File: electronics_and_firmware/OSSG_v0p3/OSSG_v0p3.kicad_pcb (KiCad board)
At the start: 4 copper layers, 85 x 9 mm, 61 parts, among them IC1 DW01A, J1 USB_B_Micro, Q1 FS8205A, Q2 Q_NPN_BEC, Q3 Q_NPN_BEC, SW1 SW_SPST, U1 ESP32-PICO-D4, U2 TP4056, U3 XC6222B331MRG, U4 FT232RQ

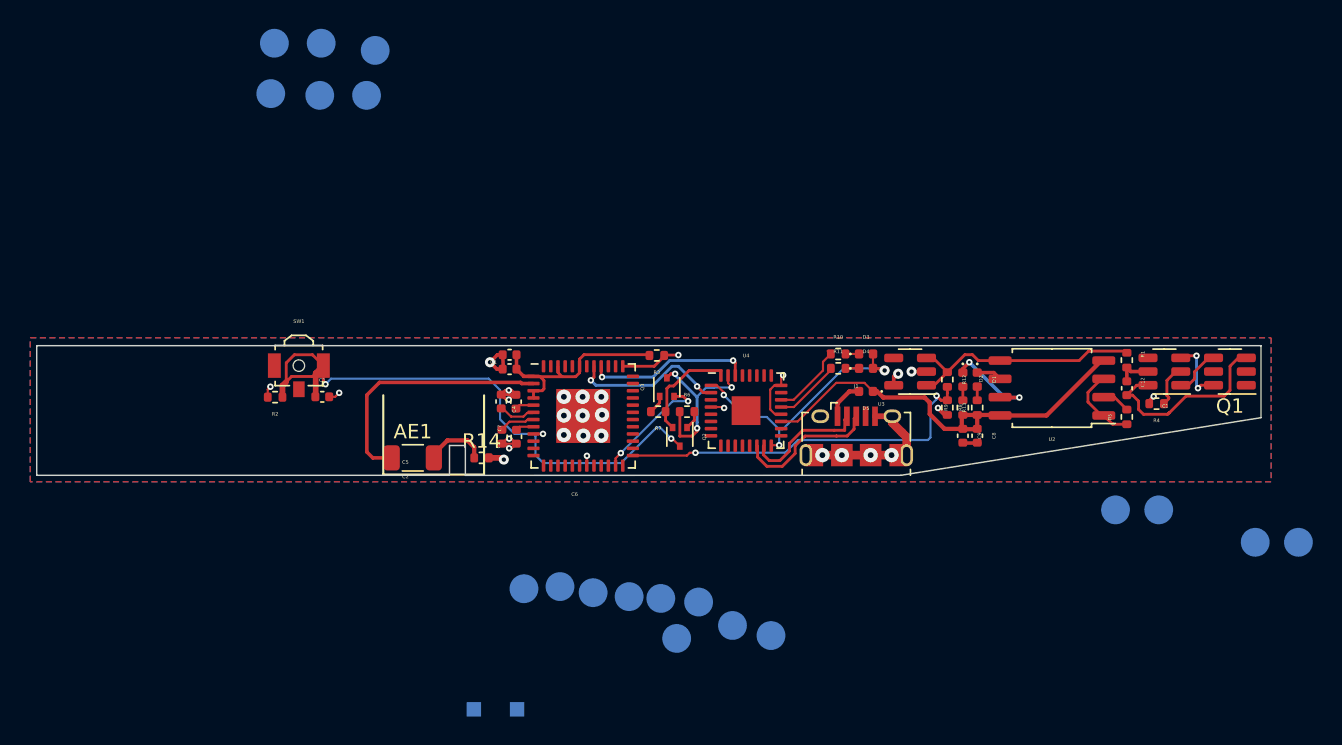
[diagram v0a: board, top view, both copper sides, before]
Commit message: change breakout test pads footprint size and start laying out breakouts
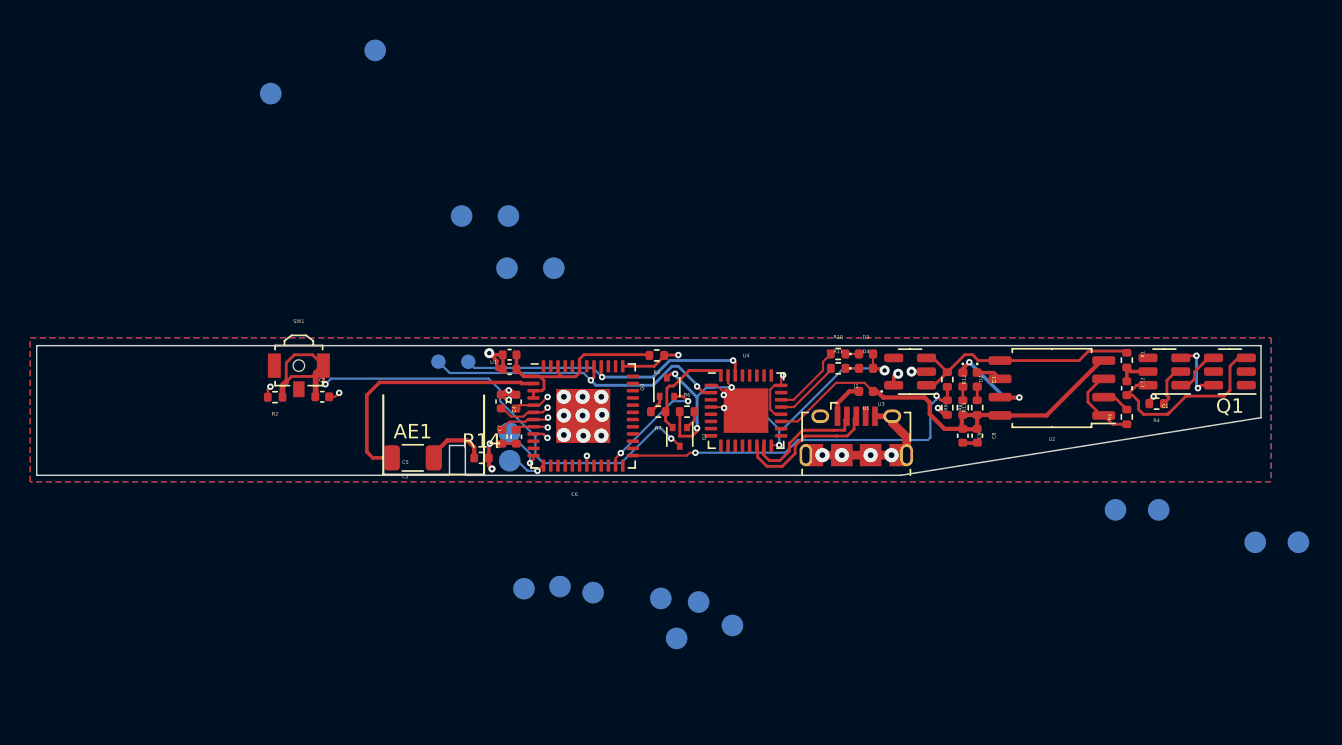
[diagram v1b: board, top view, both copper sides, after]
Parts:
- TP22: value IO15_SPI2_MISO -> IO23_BO
- TP24: value IO17_U2TXD -> IO33_BO
- TP3, TP4: footprint TestPoint:TestPoint_Pad_1.0x1.0mm -> TestPoint:TestPoint_Pad_D1.0mm
- moved TP4 24.4 mm to (105.0, 76.1)
- moved TP3 24.3 mm to (102.9, 76.1)
- moved TP24 21.8 mm to (107.8, 83.0)
- moved TP12 17.7 mm to (110.9, 69.6)
- moved TP2 17.7 mm to (107.7, 69.6)
- moved TP10 17.7 mm to (104.5, 66.0)
- moved TP11 17.7 mm to (107.8, 66.0)
- moved TP22 14.1 mm to (107.8, 81.1)
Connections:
- TP22 pad 1: IO12 -> IO32
- TP24 pad 1: IO17 -> IO33
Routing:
- net VCCIO: track 18.8 -> 31.9 mm, vias 3 -> 7
- net DTR: track 12.2 -> 0.00 mm, vias 3 -> 0
- net TX_ESP: track 10.9 -> 22.1 mm
- net RX_ESP: track 11.4 -> 21.1 mm
- net IO32: track 0.00 -> 3.32 mm, vias 0 -> 1
- net IO33: track 0.00 -> 2.31 mm, vias 0 -> 1
- net ADC1C2: track 1.31 -> 2.53 mm, vias 0 -> 1
- net ADC1C0: track 2.60 -> 3.71 mm, vias 0 -> 1
- net ADC1C1: track 2.51 -> 3.58 mm, vias 0 -> 1
- net ADC1C3: track 1.28 -> 2.29 mm, vias 0 -> 1
- net GND: track 36.9 -> 36.7 mm, vias 25 -> 23

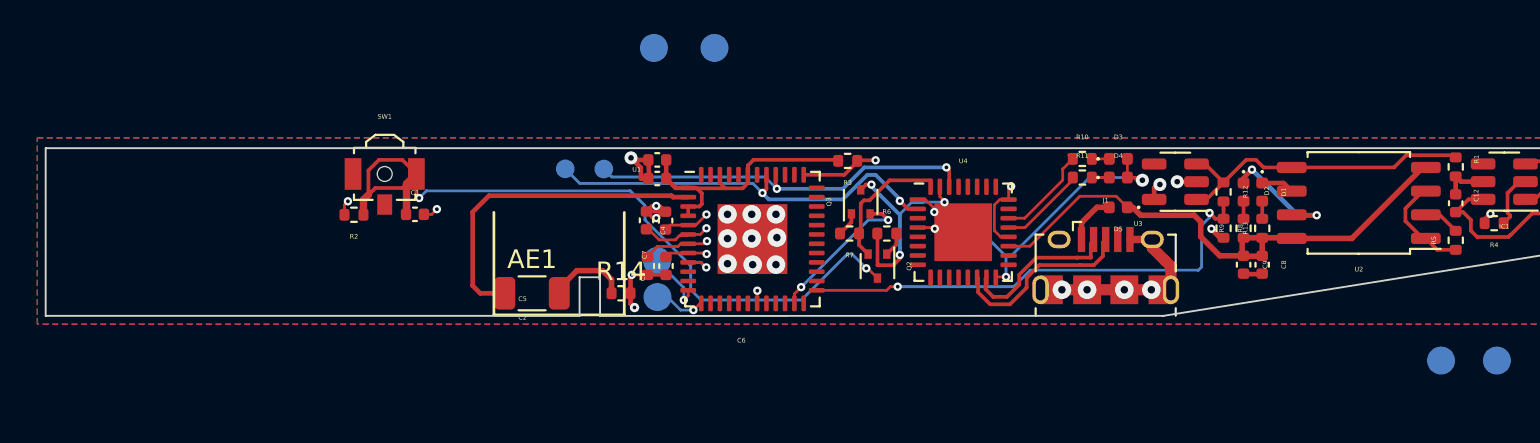
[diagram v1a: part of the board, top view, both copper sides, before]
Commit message: add voltage supervisor, go back to PRO_OB_440 antenna, more layout
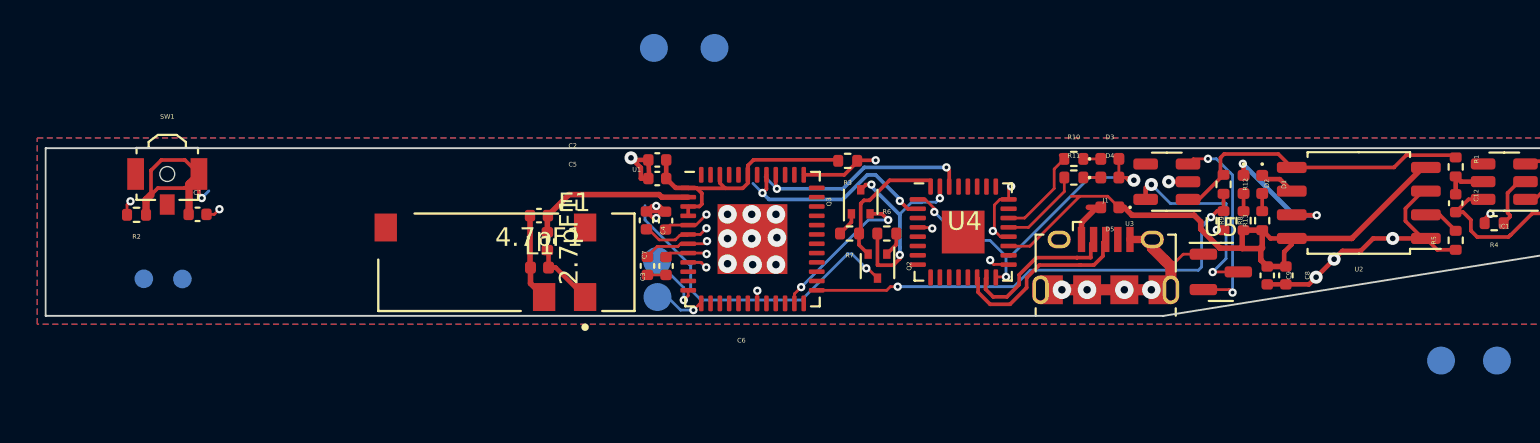
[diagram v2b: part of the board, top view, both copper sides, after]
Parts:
- removed AE1: H2U34W1H1Z0400, Resistor_SMD:R_1206_3216Metric
- removed R14: NC, Resistor_SMD:R_0402_1005Metric
- added 2.7pF1: C?, Capacitor_SMD:C_0402_1005Metric, F.Cu at (101.9, 80.0)
- added 4.7pF1: C?, Capacitor_SMD:C_0402_1005Metric, F.Cu at (101.5, 78.6)
- added E1: PRO-OB-440, OpenSourceSmartGlasses:PRO_OB_440_antenna, F.Cu at (99.9, 81.3)
- added L1: 1.6nH, Inductor_SMD:L_0402_1005Metric, F.Cu at (101.5, 81.4)
- added U5: APX803L-29SA-7, Package_TO_SOT_SMD:SOT-23, F.Cu at (138.1, 81.6)
- U4: footprint Package_DFN_QFN:QFN-32-1EP_5x5mm_P0.5mm_EP3.1x3.1mm -> OpenSourceSmartGlasses:QFN32_5mmx5mm_smallEP
- moved TP3 23.4 mm to (80.3, 82.0)
- moved TP4 23.4 mm to (82.3, 82.0)
- moved C1 11.7 mm to (83.2, 78.6)
- moved SW1 11.7 mm to (81.5, 77.2)
- moved R2 11.7 mm to (79.9, 78.6)
- moved C8 1.39 mm to (141.6, 81.8)
- moved C9 1.39 mm to (140.6, 81.8)
- moved D3 0.46 mm to (132.1, 75.6)
- moved D4 0.46 mm to (132.1, 76.6)
- moved R10 0.46 mm to (130.2, 75.6)
- moved R11 0.46 mm to (130.2, 76.6)
- moved D5 0.46 mm to (132.1, 78.2)
- moved U3 0.46 mm to (135.2, 76.8)
- moved D1 0.41 mm to (140.3, 76.9)
- moved D2 0.41 mm to (139.3, 76.9)
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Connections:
- U3 pad 3: BATT+ -> PSEN
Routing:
- net VCCIO: track 31.9 -> 18.8 mm, vias 7 -> 3
- net EN: track 43.8 -> 31.7 mm
- net GND: track 36.7 -> 48.5 mm, vias 23 -> 27
- net DTR: track 0.00 -> 11.7 mm, vias 0 -> 3
- net PSEN: track 0.00 -> 11.3 mm, vias 0 -> 2
- net TX_ESP: track 22.1 -> 11.7 mm
- net +3V3: track 7.35 -> 17.1 mm, vias 4 -> 5
- net Net-(U1-Pad2): track 18.0 -> 8.96 mm
- net RX_ESP: track 21.1 -> 12.3 mm
- net Net-(4.7pF1-Pad2): track 0.00 -> 4.68 mm
- net Net-(AE1-Pad2): track 4.40 -> 0.00 mm
- net VCC_IN: track 30.1 -> 34.2 mm
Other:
- outline, holes or cut-outs redrawn

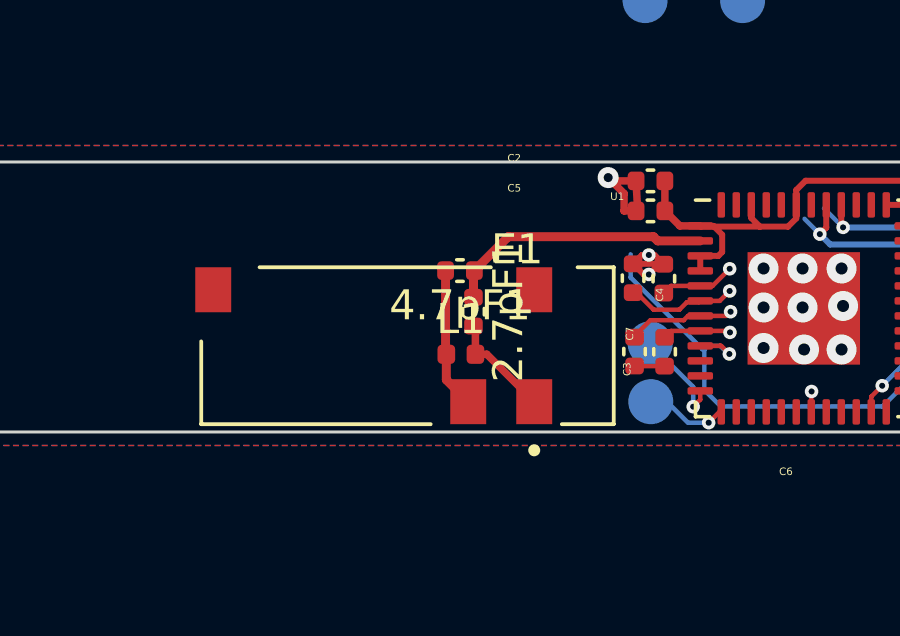
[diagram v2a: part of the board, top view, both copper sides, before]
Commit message: change antenna to 3D chip antenna
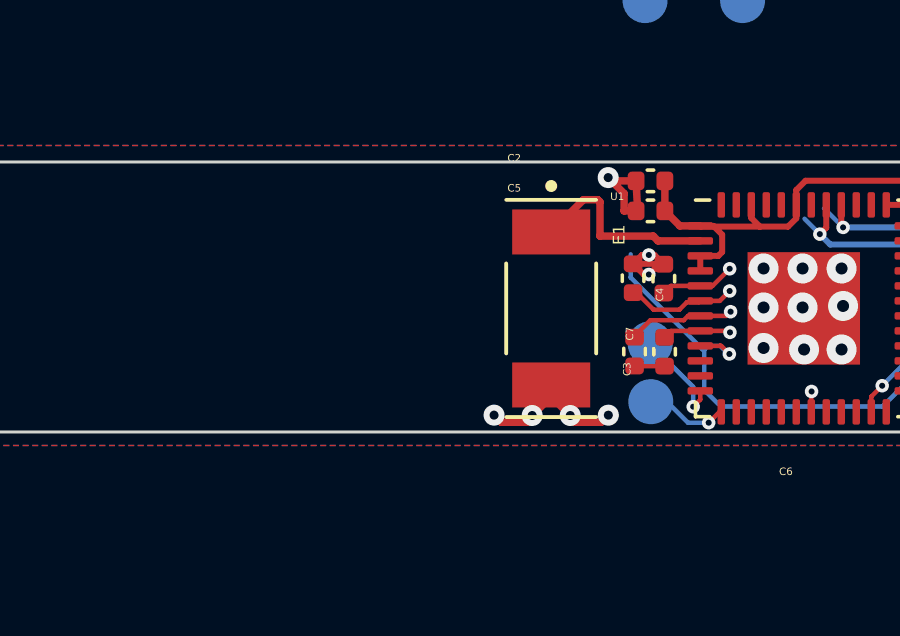
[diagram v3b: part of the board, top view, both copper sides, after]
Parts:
- removed 2.7pF1, 4.7pF1: C?, Capacitor_SMD:C_0402_1005Metric
- removed L1: 1.6nH, Inductor_SMD:L_0402_1005Metric
- E1: value PRO-OB-440 -> NN01-102; footprint OpenSourceSmartGlasses:PRO_OB_440_antenna -> OSSG_v0p3-backups:XCVR_NN01-102
- moved E1 4.80 mm to (104.5, 79.9), turned to -90 degrees
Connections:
- E1 pad 1: GND -> Net-(U1-Pad2)
- E1 pad 2: Net-(4.7pF1-Pad2) -> GND
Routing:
- net Net-(4.7pF1-Pad2): track 4.68 -> 0.00 mm
- net Net-(U1-Pad2): track 8.96 -> 6.65 mm
- net GND: track 48.5 -> 50.2 mm, vias 27 -> 31

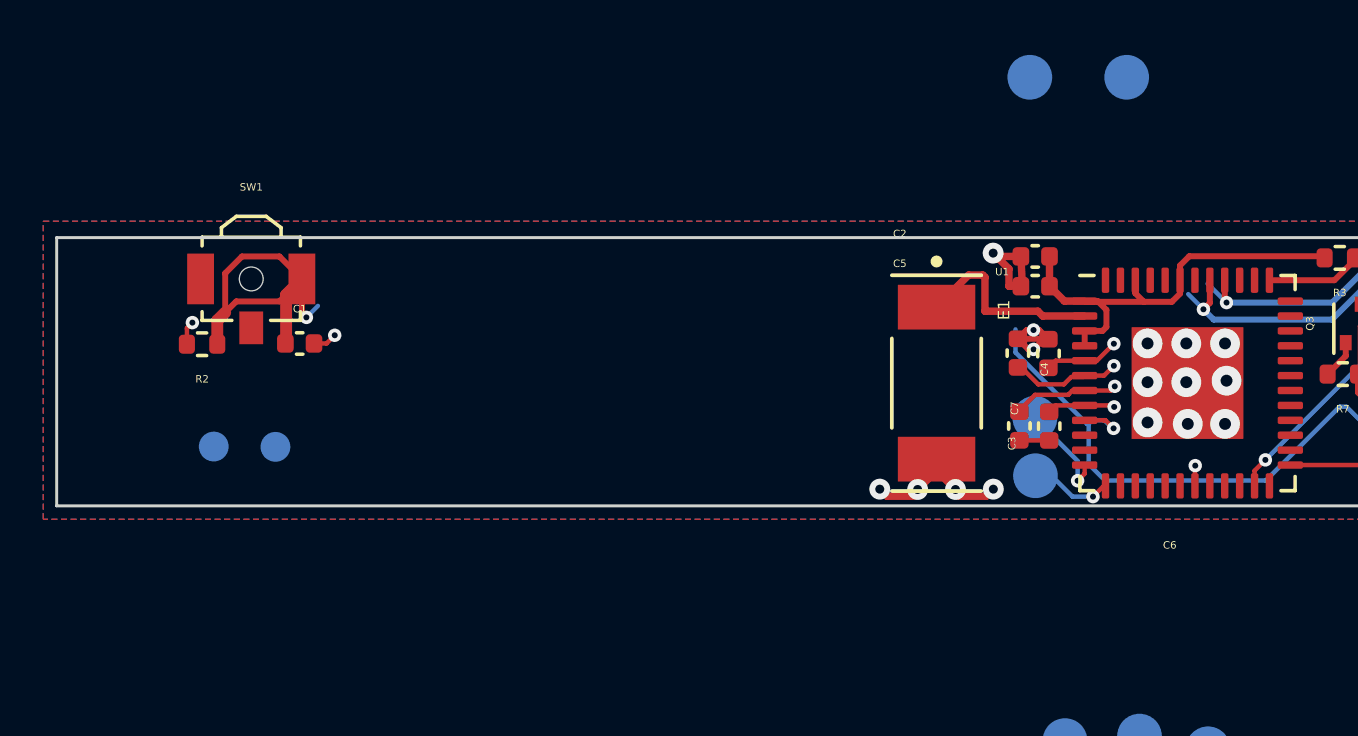
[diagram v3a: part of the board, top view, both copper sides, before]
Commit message: return to H2U34W1H1Z0400 chip antenna
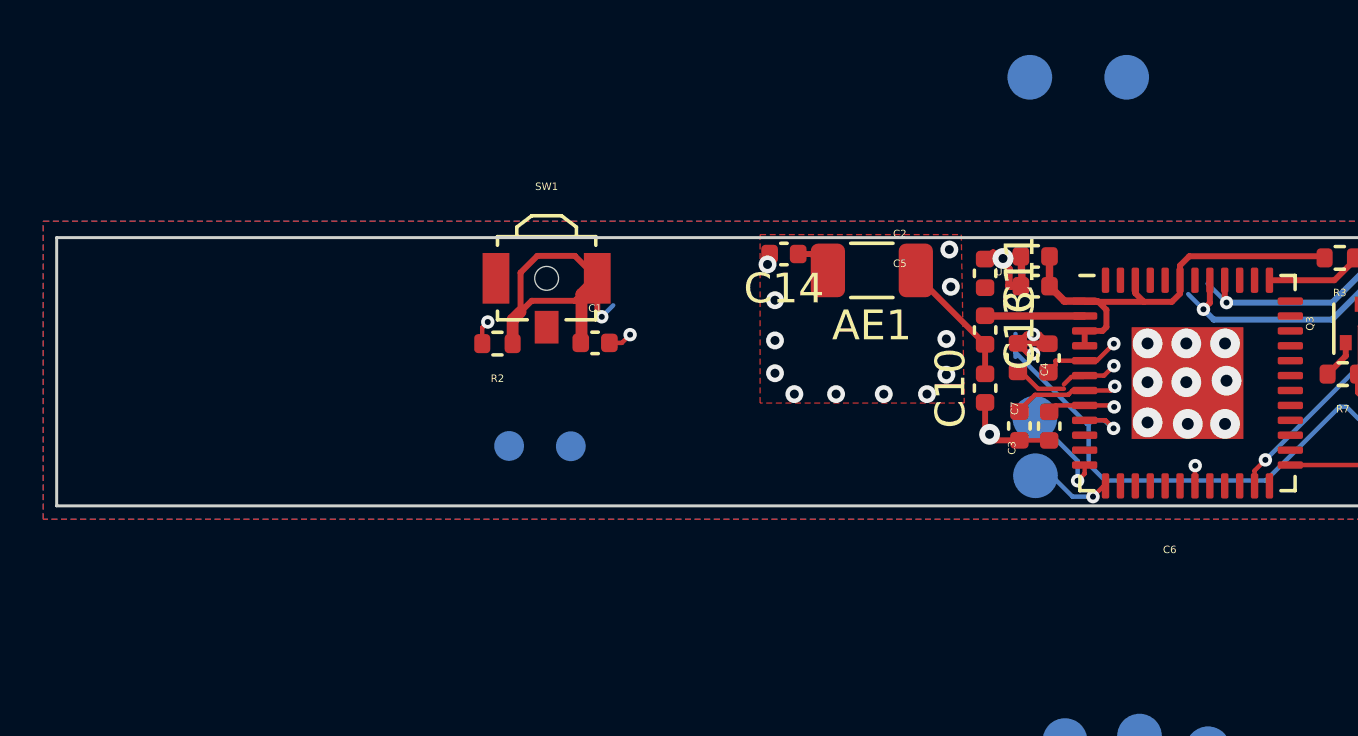
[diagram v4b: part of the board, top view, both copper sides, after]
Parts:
- removed E1: NN01-102, OSSG_v0p3-backups:XCVR_NN01-102
- added AE1: Antenna_Chip, Capacitor_SMD:C_1206_3216Metric, F.Cu at (102.3, 76.1)
- added C10: C_Small, Capacitor_SMD:C_0402_1005Metric, F.Cu at (106.2, 80.0)
- added C11: C_Small, Capacitor_SMD:C_0402_1005Metric, F.Cu at (106.2, 76.2)
- added C13: C_Small, Capacitor_SMD:C_0402_1005Metric, F.Cu at (106.2, 78.1)
- added C14: C_Small, Capacitor_SMD:C_0402_1005Metric, F.Cu at (99.4, 75.5)
- moved TP3 9.91 mm to (90.2, 82.0)
- moved C1 9.91 mm to (93.1, 78.5)
- moved R2 9.91 mm to (89.8, 78.6)
- moved SW1 9.91 mm to (91.4, 77.2)
- moved TP4 9.91 mm to (92.2, 82.0)
- moved C3 0.15 mm to (107.2, 79.0)
- moved C6 0.15 mm to (108.3, 79.0)
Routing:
- net Net-(AE1-Pad1): track 0.00 -> 4.76 mm
- net Net-(U1-Pad2): track 6.65 -> 3.34 mm
- net GND: track 50.2 -> 47.9 mm, vias 31 -> 40
- net Net-(AE1-Pad2): track 0.00 -> 1.22 mm
